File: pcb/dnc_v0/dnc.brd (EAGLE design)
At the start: 100 x 83.2 mm, 70 parts, among them Q5 TSM2306CX, Q7 TSM2306CX, Q8 TSM2306CX

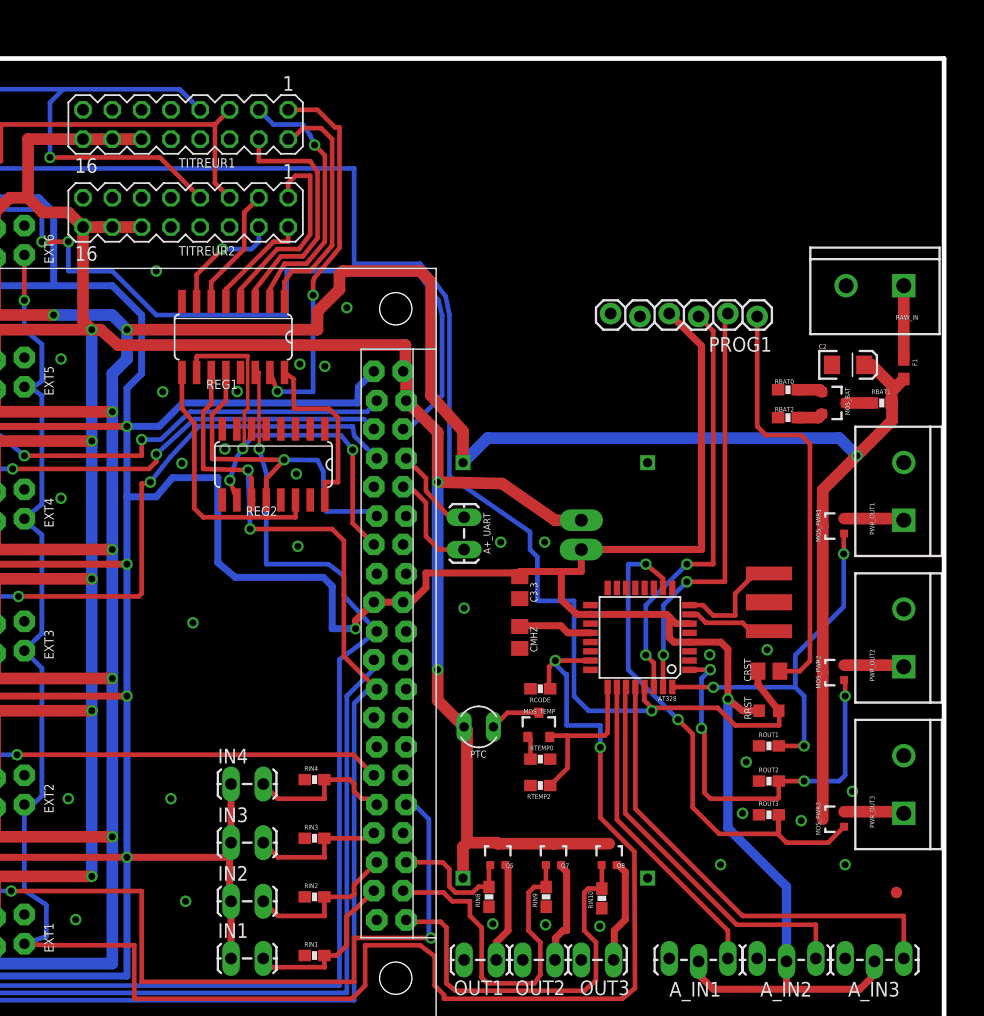
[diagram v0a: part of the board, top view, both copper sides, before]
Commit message: Update lib and clean up the brd
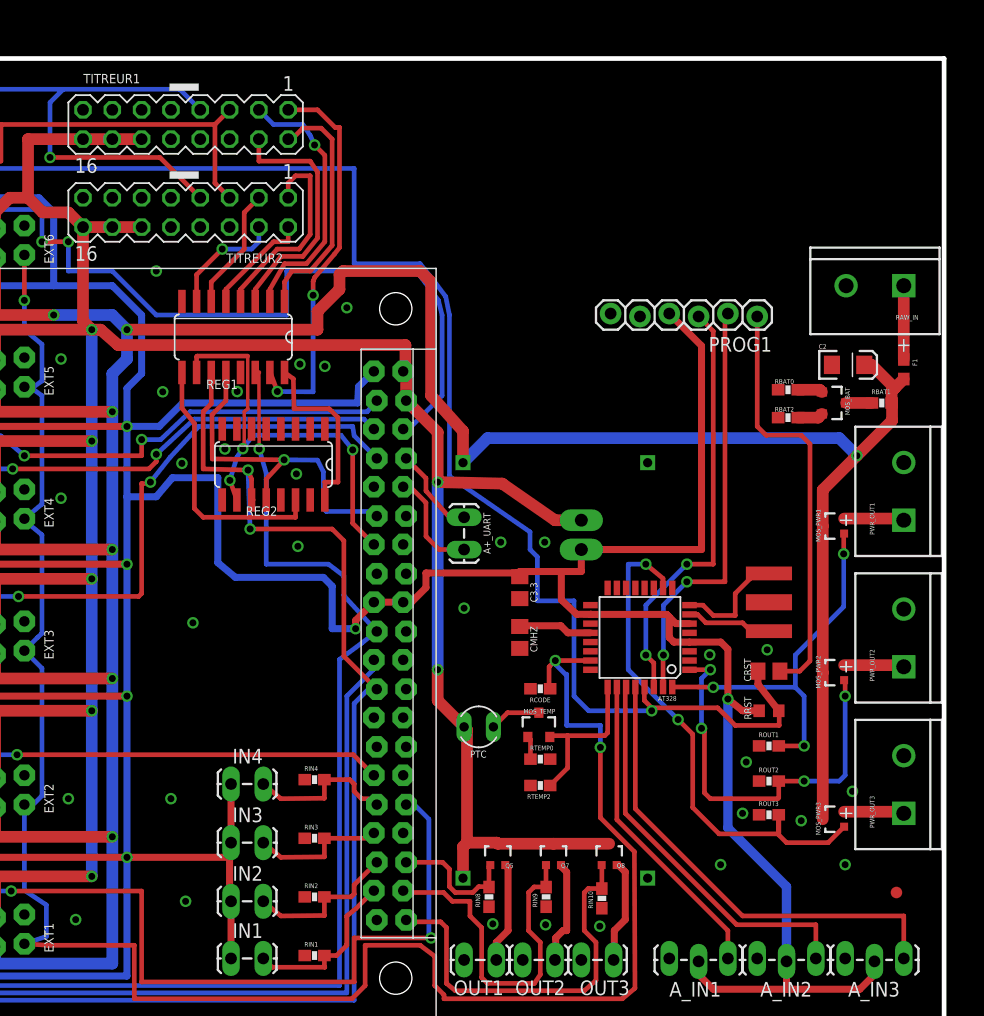
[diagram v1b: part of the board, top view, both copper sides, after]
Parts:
- A_IN1, A_IN2, A_IN3: value (none) -> DNC_IN3; device SparkFun:1X03_LOCK_LONGPADS -> pierre_vv:DNC_IN3
- IN1, IN2, IN3, IN4: value (none) -> DNC_IN2; device SparkFun:1X02_LOCK_LONGPADS -> pierre_vv:DNC_IN2
- OUT1, OUT2, OUT3: value M02LOCK_LONGPADS -> DNC_IN2; device SparkFun-Connectors:1X02_LOCK_LONGPADS -> pierre_vv:DNC_IN2
- PWR_OUT1, PWR_OUT2, PWR_OUT3, RAW_IN: value M025MM -> DNC_IN2PWR; device SparkFun-Connectors:SCREWTERMINAL-5MM-2 -> pierre_vv:DNC_IN2_PWR
- TITREUR1, TITREUR2: value (none) -> DNC_TITREUR; device con-lstb:MA08-2 -> pierre_vv:DNC_TITREUR

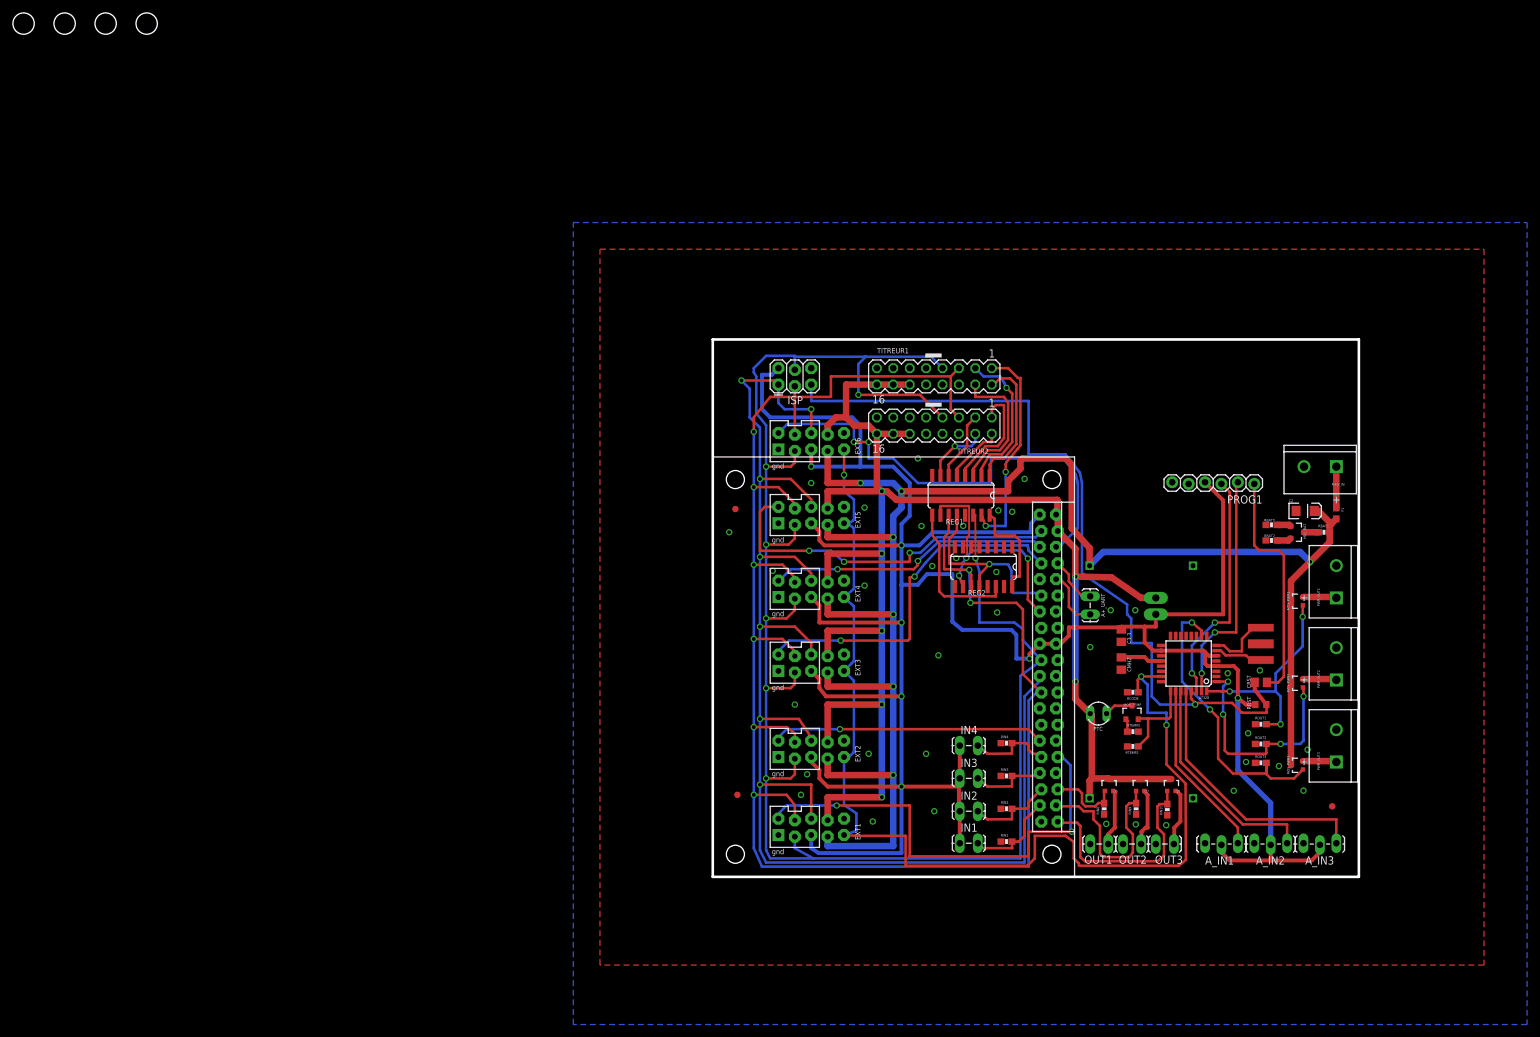
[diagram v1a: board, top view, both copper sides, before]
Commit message: Finished brd before first print
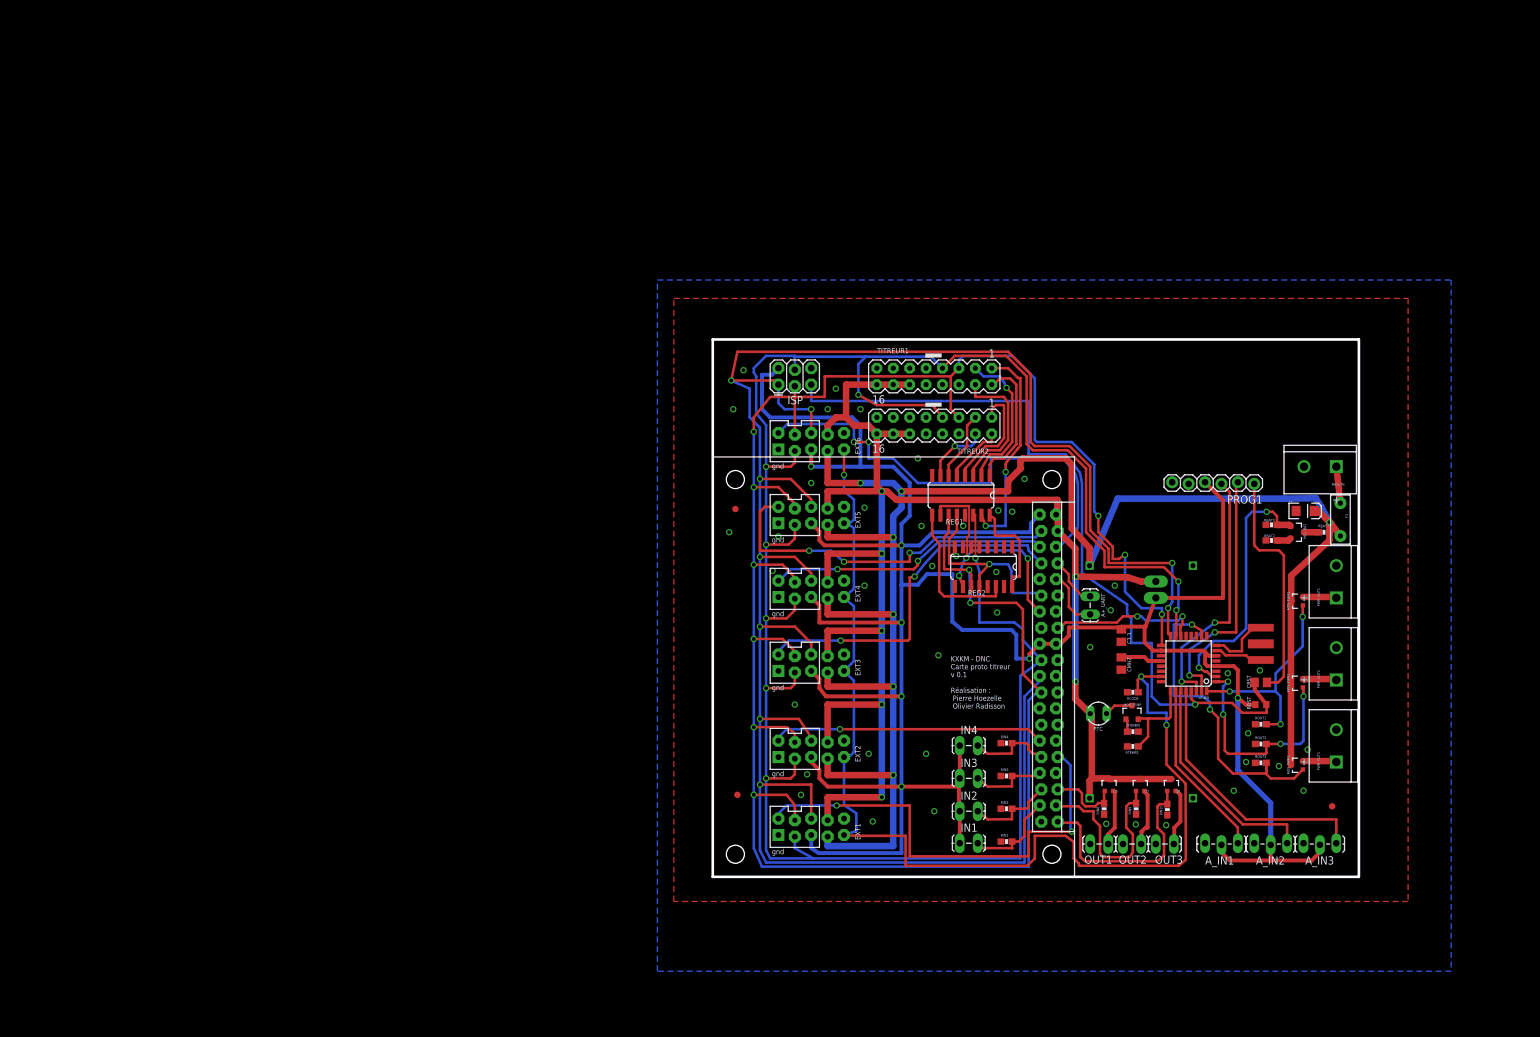
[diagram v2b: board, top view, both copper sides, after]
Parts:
- removed JP15, JP16, JP17, JP18: STAND-OFF, SparkFun:STAND-OFF
- F1: value PTC0603 -> PTCPTH; device SparkFun-PowerIC:0603 -> SparkFun-PowerIC:PTC
- moved 3.3/5 2.54 mm to (68.6, 43.2)
- moved F1 1.14 mm to (97.2, 55.3)
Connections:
- net ACTIVE_ANALOG_RAW: now also AT328.2
- net ATMEGA_CS: now also AT328.14
- net MISO: now also AT328.16
- net MOSI: now also AT328.15
- net N$12: now also F1.P$1; no longer F1.1
- net RAW: now also F1.P$2; no longer F1.2
- net SCK: now also AT328.17
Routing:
- net MISO: track 218.5 -> 331.6 mm, vias 7 -> 9
- net MOSI: track 270.3 -> 343.9 mm, vias 7 -> 9
- net SCK: track 275.2 -> 346.4 mm, vias 8 -> 11
- net ACTIVE_ANALOG_RAW: track 2.17 -> 40.3 mm, vias 0 -> 2
- net ATMEGA_CS: track 0.00 -> 23.7 mm, vias 0 -> 2
- net RAW: track 261.1 -> 273.0 mm
- net ACTIVE_OUT_POWER_3: track 45.9 -> 49.9 mm
- net TX-O: track 36.6 -> 39.7 mm
- net RX-I: track 36.7 -> 39.7 mm
- net +3V3: track 404.3 -> 403.0 mm
- net +5V: track 251.6 -> 250.7 mm
- net N$12: track 6.39 -> 5.69 mm
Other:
- board text added: "KXKM - DNC Carte proto titreur v 0.1 Réalisation : Pierre Hoezelle Olivier Radisson"

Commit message: commande pcb passée
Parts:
- moved F1 0.64 mm to (96.5, 55.3)
- moved RAW_IN 0.45 mm to (96.2, 63.8)
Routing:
- net CODE: track 173.1 -> 170.9 mm
- net SCK: track 346.4 -> 344.6 mm
- net MOSI: track 343.9 -> 342.0 mm
- net MISO: track 331.6 -> 329.7 mm
- net /CS_EXT_1: track 71.3 -> 69.8 mm
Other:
- board size 100 x 83.2 mm -> 98.7 x 83.2 mm
